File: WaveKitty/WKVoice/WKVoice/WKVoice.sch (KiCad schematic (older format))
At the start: 65 parts, among them J1 Conn, J2 Debug, J3 AudioJack3, J4 Conn_01x03, U1 ATmega328P-PU, U2 LM358, U3 LM358, Y1 Crystal

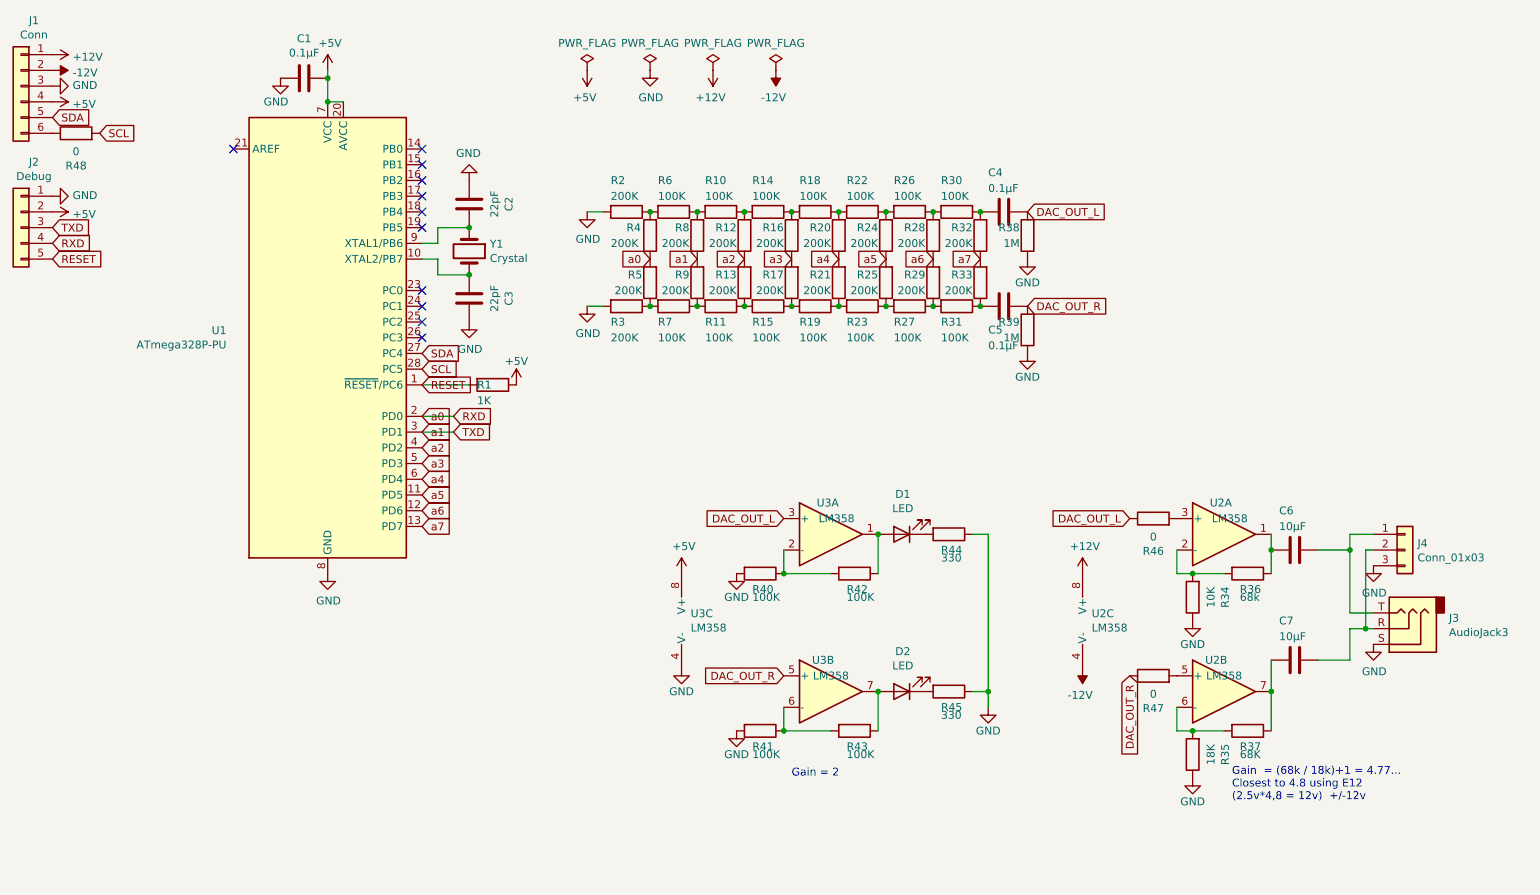
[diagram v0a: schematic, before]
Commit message: Initial work on BitBug
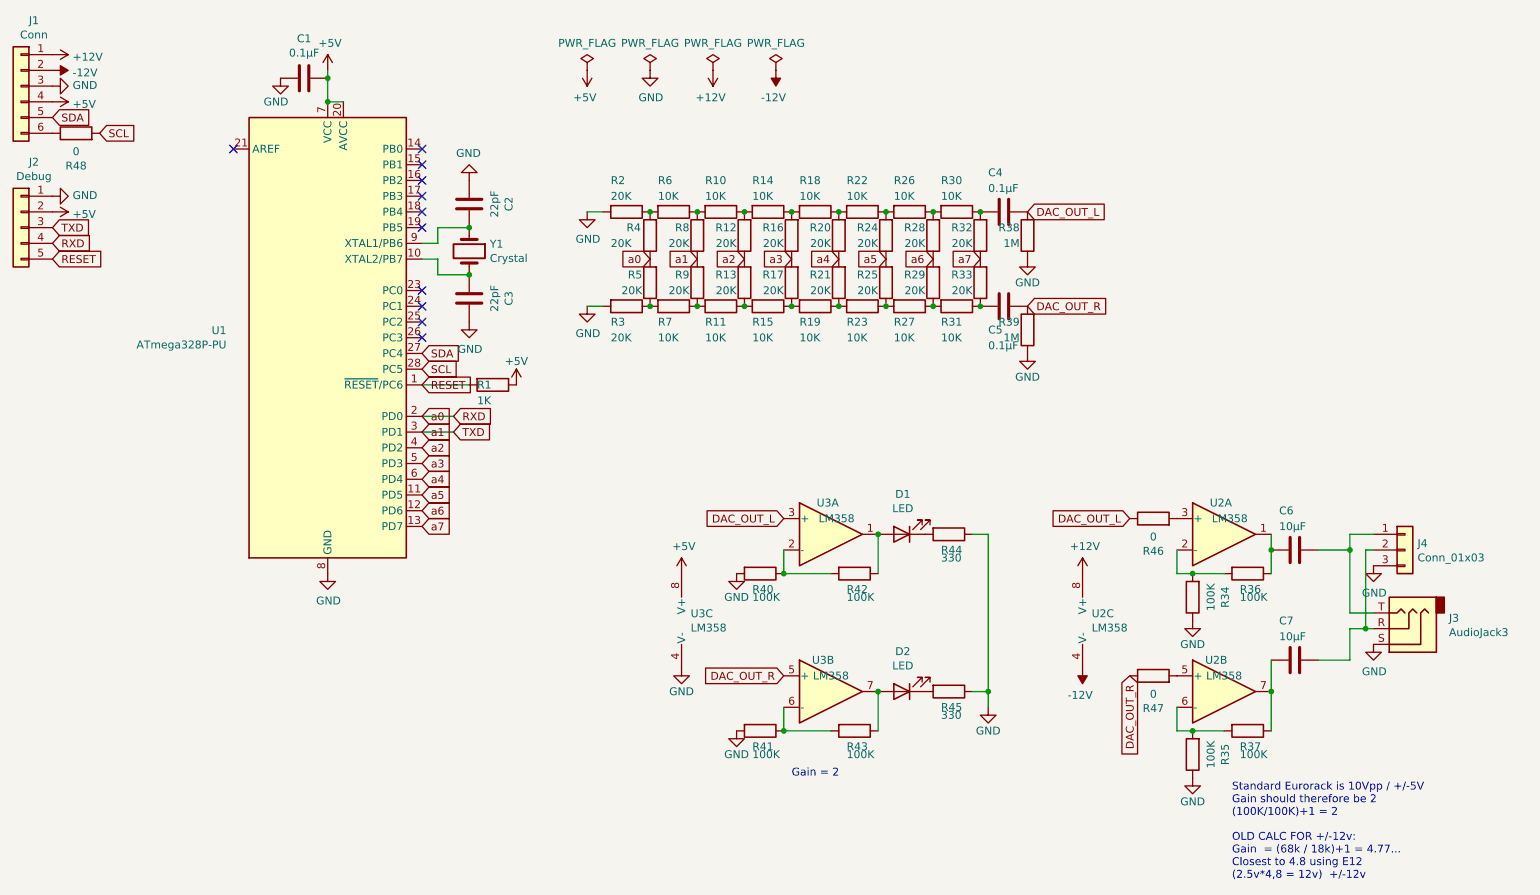
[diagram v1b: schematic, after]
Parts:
- R10, R11, R14, R15, R18, R19, R22, R23, R26, R27, R30, R31, R6, R7: value 100K -> 10K
- R12, R13, R16, R17, R2, R20, R21, R24, R25, R28, R29, R3, R32, R33, R4, R5, R8, R9: value 200K -> 20K
- R34: value 10K -> 100K
- R35: value 18K -> 100K
- R36: value 68k -> 100K
- R37: value 68K -> 100K
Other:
- note added: "OLD CALC FOR +/-12v:\nGain = (68k / 18k)+1 = 4.77...\nClosest to 4.8 using E12\n(2.5v*4,8 = 12v) ~ +/-12v"
- note added: "Standard Eurorack is 10Vpp / +/-5V\nGain should therefore be 2\n(100K/100K)+1 = 2"
- note removed: "Gain = (68k / 18k)+1 = 4.77...\nClosest to 4.8 using E12\n(2.5v*4,8 = 12v) ~ +/-12v"
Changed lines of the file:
@@
 P 5000 2550
 F 0 "R7" V 5100 2450 50  0000 L CNN
-F 1 "100K" V 5200 2450 50  0000 L CNN
+F 1 "10K" V 5200 2450 50  0000 L CNN
 F 2 "Resistor_THT:R_Axial_DIN0207_L6.3mm_D2.5mm_P10.16mm_Horizontal" V 4930 2550 50  0001 C CNN
 F 3 "~" H 5000 2550 50  0001 C CNN
@@
 P 5450 2400
 F 0 "R13" H 5500 2350 50  0000 L CNN
-F 1 "200K" H 5500 2450 50  0000 L CNN
+F 1 "20K" H 5500 2450 50  0000 L CNN
 F 2 "Resistor_THT:R_Axial_DIN0207_L6.3mm_D2.5mm_P10.16mm_Horizontal" V 5380 2400 50  0001 C CNN
 F 3 "~" H 5450 2400 50  0001 C CNN
@@
 P 5750 2400
 F 0 "R17" H 5800 2350 50  0000 L CNN
-F 1 "200K" H 5800 2450 50  0000 L CNN
+F 1 "20K" H 5800 2450 50  0000 L CNN
 F 2 "Resistor_THT:R_Axial_DIN0207_L6.3mm_D2.5mm_P10.16mm_Horizontal" V 5680 2400 50  0001 C CNN
 F 3 "~" H 5750 2400 50  0001 C CNN
@@
 P 6050 2400
 F 0 "R21" H 6100 2350 50  0000 L CNN
-F 1 "200K" H 6100 2450 50  0000 L CNN
+F 1 "20K" H 6100 2450 50  0000 L CNN
 F 2 "Resistor_THT:R_Axial_DIN0207_L6.3mm_D2.5mm_P10.16mm_Horizontal" V 5980 2400 50  0001 C CNN
 F 3 "~" H 6050 2400 50  0001 C CNN
@@
 P 6350 2400
 F 0 "R25" H 6400 2350 50  0000 L CNN
-F 1 "200K" H 6400 2450 50  0000 L CNN
+F 1 "20K" H 6400 2450 50  0000 L CNN
 F 2 "Resistor_THT:R_Axial_DIN0207_L6.3mm_D2.5mm_P10.16mm_Horizontal" V 6280 2400 50  0001 C CNN
 F 3 "~" H 6350 2400 50  0001 C CNN
@@
 P 6650 2400
 F 0 "R29" H 6700 2350 50  0000 L CNN
-F 1 "200K" H 6700 2450 50  0000 L CNN
+F 1 "20K" H 6700 2450 50  0000 L CNN
 F 2 "Resistor_THT:R_Axial_DIN0207_L6.3mm_D2.5mm_P10.16mm_Horizontal" V 6580 2400 50  0001 C CNN
 F 3 "~" H 6650 2400 50  0001 C CNN
@@
 P 6950 2400
 F 0 "R33" H 7000 2350 50  0000 L CNN
-F 1 "200K" H 7000 2450 50  0000 L CNN
+F 1 "20K" H 7000 2450 50  0000 L CNN
 F 2 "Resistor_THT:R_Axial_DIN0207_L6.3mm_D2.5mm_P10.16mm_Horizontal" V 6880 2400 50  0001 C CNN
 F 3 "~" H 6950 2400 50  0001 C CNN
@@
 P 5300 2550
 F 0 "R11" V 5400 2450 50  0000 L CNN
-F 1 "100K" V 5500 2450 50  0000 L CNN
+F 1 "10K" V 5500 2450 50  0000 L CNN
 F 2 "Resistor_THT:R_Axial_DIN0207_L6.3mm_D2.5mm_P10.16mm_Horizontal" V 5230 2550 50  0001 C CNN
 F 3 "~" H 5300 2550 50  0001 C CNN
@@
 P 5600 2550
 F 0 "R15" V 5700 2450 50  0000 L CNN
-F 1 "100K" V 5800 2450 50  0000 L CNN
+F 1 "10K" V 5800 2450 50  0000 L CNN
 F 2 "Resistor_THT:R_Axial_DIN0207_L6.3mm_D2.5mm_P10.16mm_Horizontal" V 5530 2550 50  0001 C CNN
 F 3 "~" H 5600 2550 50  0001 C CNN
@@
 P 5900 2550
 F 0 "R19" V 6000 2450 50  0000 L CNN
-F 1 "100K" V 6100 2450 50  0000 L CNN
+F 1 "10K" V 6100 2450 50  0000 L CNN
 F 2 "Resistor_THT:R_Axial_DIN0207_L6.3mm_D2.5mm_P10.16mm_Horizontal" V 5830 2550 50  0001 C CNN
 F 3 "~" H 5900 2550 50  0001 C CNN
@@
 P 6200 2550
 F 0 "R23" V 6300 2450 50  0000 L CNN
-F 1 "100K" V 6400 2450 50  0000 L CNN
+F 1 "10K" V 6400 2450 50  0000 L CNN
 F 2 "Resistor_THT:R_Axial_DIN0207_L6.3mm_D2.5mm_P10.16mm_Horizontal" V 6130 2550 50  0001 C CNN
 F 3 "~" H 6200 2550 50  0001 C CNN
@@
 P 6500 2550
 F 0 "R27" V 6600 2450 50  0000 L CNN
-F 1 "100K" V 6700 2450 50  0000 L CNN
+F 1 "10K" V 6700 2450 50  0000 L CNN
 F 2 "Resistor_THT:R_Axial_DIN0207_L6.3mm_D2.5mm_P10.16mm_Horizontal" V 6430 2550 50  0001 C CNN
 F 3 "~" H 6500 2550 50  0001 C CNN
@@
 P 6800 2550
 F 0 "R31" V 6900 2450 50  0000 L CNN
-F 1 "100K" V 7000 2450 50  0000 L CNN
+F 1 "10K" V 7000 2450 50  0000 L CNN
 F 2 "Resistor_THT:R_Axial_DIN0207_L6.3mm_D2.5mm_P10.16mm_Horizontal" V 6730 2550 50  0001 C CNN
 F 3 "~" H 6800 2550 50  0001 C CNN
@@
 P 5000 1950
 F 0 "R6" V 4800 1850 50  0000 L CNN
-F 1 "100K" V 4900 1850 50  0000 L CNN
+F 1 "10K" V 4900 1850 50  0000 L CNN
 F 2 "Resistor_THT:R_Axial_DIN0207_L6.3mm_D2.5mm_P10.16mm_Horizontal" V 4930 1950 50  0001 C CNN
 F 3 "~" H 5000 1950 50  0001 C CNN
@@
 P 5300 1950
 F 0 "R10" V 5100 1850 50  0000 L CNN
-F 1 "100K" V 5200 1850 50  0000 L CNN
+F 1 "10K" V 5200 1850 50  0000 L CNN
 F 2 "Resistor_THT:R_Axial_DIN0207_L6.3mm_D2.5mm_P10.16mm_Horizontal" V 5230 1950 50  0001 C CNN
 F 3 "~" H 5300 1950 50  0001 C CNN
@@
 P 5600 1950
 F 0 "R14" V 5400 1850 50  0000 L CNN
-F 1 "100K" V 5500 1850 50  0000 L CNN
+F 1 "10K" V 5500 1850 50  0000 L CNN
 F 2 "Resistor_THT:R_Axial_DIN0207_L6.3mm_D2.5mm_P10.16mm_Horizontal" V 5530 1950 50  0001 C CNN
 F 3 "~" H 5600 1950 50  0001 C CNN
@@
 P 5900 1950
 F 0 "R18" V 5700 1850 50  0000 L CNN
-F 1 "100K" V 5800 1850 50  0000 L CNN
+F 1 "10K" V 5800 1850 50  0000 L CNN
 F 2 "Resistor_THT:R_Axial_DIN0207_L6.3mm_D2.5mm_P10.16mm_Horizontal" V 5830 1950 50  0001 C CNN
 F 3 "~" H 5900 1950 50  0001 C CNN
@@
 P 6200 1950
 F 0 "R22" V 6000 1850 50  0000 L CNN
-F 1 "100K" V 6100 1850 50  0000 L CNN
+F 1 "10K" V 6100 1850 50  0000 L CNN
 F 2 "Resistor_THT:R_Axial_DIN0207_L6.3mm_D2.5mm_P10.16mm_Horizontal" V 6130 1950 50  0001 C CNN
 F 3 "~" H 6200 1950 50  0001 C CNN
@@
 P 6800 1950
 F 0 "R30" V 6600 1850 50  0000 L CNN
-F 1 "100K" V 6700 1850 50  0000 L CNN
+F 1 "10K" V 6700 1850 50  0000 L CNN
 F 2 "Resistor_THT:R_Axial_DIN0207_L6.3mm_D2.5mm_P10.16mm_Horizontal" V 6730 1950 50  0001 C CNN
 F 3 "~" H 6800 1950 50  0001 C CNN
@@
 P 6950 2100
 F 0 "R32" H 7000 2050 50  0000 L CNN
-F 1 "200K" H 7000 2150 50  0000 L CNN
+F 1 "20K" H 7000 2150 50  0000 L CNN
 F 2 "Resistor_THT:R_Axial_DIN0207_L6.3mm_D2.5mm_P10.16mm_Horizontal" V 6880 2100 50  0001 C CNN
 F 3 "~" H 6950 2100 50  0001 C CNN
@@
 P 6650 2100
 F 0 "R28" H 6700 2050 50  0000 L CNN
-F 1 "200K" H 6700 2150 50  0000 L CNN
+F 1 "20K" H 6700 2150 50  0000 L CNN
 F 2 "Resistor_THT:R_Axial_DIN0207_L6.3mm_D2.5mm_P10.16mm_Horizontal" V 6580 2100 50  0001 C CNN
 F 3 "~" H 6650 2100 50  0001 C CNN
@@
 P 6350 2100
 F 0 "R24" H 6400 2050 50  0000 L CNN
-F 1 "200K" H 6400 2150 50  0000 L CNN
+F 1 "20K" H 6400 2150 50  0000 L CNN
 F 2 "Resistor_THT:R_Axial_DIN0207_L6.3mm_D2.5mm_P10.16mm_Horizontal" V 6280 2100 50  0001 C CNN
 F 3 "~" H 6350 2100 50  0001 C CNN
@@
 P 6050 2100
 F 0 "R20" H 6100 2050 50  0000 L CNN
-F 1 "200K" H 6100 2150 50  0000 L CNN
+F 1 "20K" H 6100 2150 50  0000 L CNN
 F 2 "Resistor_THT:R_Axial_DIN0207_L6.3mm_D2.5mm_P10.16mm_Horizontal" V 5980 2100 50  0001 C CNN
 F 3 "~" H 6050 2100 50  0001 C CNN
@@
 P 5450 2100
 F 0 "R12" H 5500 2050 50  0000 L CNN
-F 1 "200K" H 5500 2150 50  0000 L CNN
+F 1 "20K" H 5500 2150 50  0000 L CNN
 F 2 "Resistor_THT:R_Axial_DIN0207_L6.3mm_D2.5mm_P10.16mm_Horizontal" V 5380 2100 50  0001 C CNN
 F 3 "~" H 5450 2100 50  0001 C CNN
@@
 P 5150 2100
 F 0 "R8" H 5200 2050 50  0000 L CNN
-F 1 "200K" H 5200 2150 50  0000 L CNN
+F 1 "20K" H 5200 2150 50  0000 L CNN
 F 2 "Resistor_THT:R_Axial_DIN0207_L6.3mm_D2.5mm_P10.16mm_Horizontal" V 5080 2100 50  0001 C CNN
 F 3 "~" H 5150 2100 50  0001 C CNN
@@
 P 8650 5250
 F 0 "R37" V 8750 5200 50  0000 L CNN
-F 1 "68K" V 8800 5200 50  0000 L CNN
+F 1 "100K" V 8800 5200 50  0000 L CNN
 F 2 "Resistor_THT:R_Axial_DIN0207_L6.3mm_D2.5mm_P10.16mm_Horizontal" V 8580 5250 50  0001 C CNN
 F 3 "~" H 8650 5250 50  0001 C CNN
@@
 P 8650 4250
 F 0 "R36" V 8750 4200 50  0000 L CNN
-F 1 "68k" V 8800 4200 50  0000 L CNN
+F 1 "100K" V 8800 4200 50  0000 L CNN
 F 2 "Resistor_THT:R_Axial_DIN0207_L6.3mm_D2.5mm_P10.16mm_Horizontal" V 8580 4250 50  0001 C CNN
 F 3 "~" H 8650 4250 50  0001 C CNN
@@
 P 8300 5400
 F 0 "R35" V 8093 5400 50  0000 C CNN
-F 1 "18K" V 8184 5400 50  0000 C CNN
+F 1 "100K" V 8184 5400 50  0000 C CNN
 F 2 "Resistor_THT:R_Axial_DIN0207_L6.3mm_D2.5mm_P10.16mm_Horizontal" V 8230 5400 50  0001 C CNN
 F 3 "~" H 8300 5400 50  0001 C CNN
@@
 P 4700 2550
 F 0 "R3" V 4800 2450 50  0000 L CNN
-F 1 "200K" V 4900 2450 50  0000 L CNN
+F 1 "20K" V 4900 2450 50  0000 L CNN
 F 2 "Resistor_THT:R_Axial_DIN0207_L6.3mm_D2.5mm_P10.16mm_Horizontal" V 4630 2550 50  0001 C CNN
 F 3 "~" H 4700 2550 50  0001 C CNN
@@
 P 5750 2100
 F 0 "R16" H 5800 2050 50  0000 L CNN
-F 1 "200K" H 5800 2150 50  0000 L CNN
+F 1 "20K" H 5800 2150 50  0000 L CNN
 F 2 "Resistor_THT:R_Axial_DIN0207_L6.3mm_D2.5mm_P10.16mm_Horizontal" V 5680 2100 50  0001 C CNN
 F 3 "~" H 5750 2100 50  0001 C CNN
@@
 P 6500 1950
 F 0 "R26" V 6300 1850 50  0000 L CNN
-F 1 "100K" V 6400 1850 50  0000 L CNN
+F 1 "10K" V 6400 1850 50  0000 L CNN
 F 2 "Resistor_THT:R_Axial_DIN0207_L6.3mm_D2.5mm_P10.16mm_Horizontal" V 6430 1950 50  0001 C CNN
 F 3 "~" H 6500 1950 50  0001 C CNN
@@
 P 4700 1950
 F 0 "R2" V 4500 1850 50  0000 L CNN
-F 1 "200K" V 4600 1850 50  0000 L CNN
+F 1 "20K" V 4600 1850 50  0000 L CNN
 F 2 "Resistor_THT:R_Axial_DIN0207_L6.3mm_D2.5mm_P10.16mm_Horizontal" V 4630 1950 50  0001 C CNN
 F 3 "~" H 4700 1950 50  0001 C CNN
@@
 P 4850 2100
 F 0 "R4" H 5000 2050 50  0000 R CNN
-F 1 "200K" H 5100 2150 50  0000 R CNN
+F 1 "20K" H 5100 2150 50  0000 R CNN
 F 2 "Resistor_THT:R_Axial_DIN0207_L6.3mm_D2.5mm_P10.16mm_Horizontal" V 4780 2100 50  0001 C CNN
 F 3 "~" H 4850 2100 50  0001 C CNN
@@
 P 5150 2400
 F 0 "R9" H 5200 2350 50  0000 L CNN
-F 1 "200K" H 5200 2450 50  0000 L CNN
+F 1 "20K" H 5200 2450 50  0000 L CNN
 F 2 "Resistor_THT:R_Axial_DIN0207_L6.3mm_D2.5mm_P10.16mm_Horizontal" V 5080 2400 50  0001 C CNN
 F 3 "~" H 5150 2400 50  0001 C CNN
@@
 P 4850 2400
 F 0 "R5" H 4900 2350 50  0000 L CNN
-F 1 "200K" H 4900 2450 50  0000 L CNN
+F 1 "20K" H 4900 2450 50  0000 L CNN
 F 2 "Resistor_THT:R_Axial_DIN0207_L6.3mm_D2.5mm_P10.16mm_Horizontal" V 4780 2400 50  0001 C CNN
 F 3 "~" H 4850 2400 50  0001 C CNN
@@
 Wire Wire Line
 	8800 4100 8800 4000
-Text Notes 8550 5700 0    50   ~ 0
-Gain  = (68k / 18k)+1 = 4.77...\nClosest to 4.8 using E12\n(2.5v*4,8 = 12v) ~ +/-12v
+Text Notes 8550 6200 0    50   ~ 0
+OLD CALC FOR +/-12v:\nGain  = (68k / 18k)+1 = 4.77...\nClosest to 4.8 using E12\n(2.5v*4,8 = 12v) ~ +/-12v
 $Comp
 L Device:R R34
@@
 P 8300 4400
 F 0 "R34" V 8093 4400 50  0000 C CNN
-F 1 "10K" V 8184 4400 50  0000 C CNN
+F 1 "100K" V 8184 4400 50  0000 C CNN
 F 2 "Resistor_THT:R_Axial_DIN0207_L6.3mm_D2.5mm_P10.16mm_Horizontal" V 8230 4400 50  0001 C CNN
 F 3 "~" H 8300 4400 50  0001 C CNN
@@
 Wire Wire Line
 	9400 4600 9450 4600
+Text Notes 8550 5800 0    50   ~ 0
+Standard Eurorack is 10Vpp / +/-5V\nGain should therefore be 2\n(100K/100K)+1 = 2
 $EndSCHEMATC
